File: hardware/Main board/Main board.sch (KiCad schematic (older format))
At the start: 104 parts, among them J1 Wind Direction, J10 Free Pins, J11 Nokia 5110 LCD, J12 3v3 in, J2 Wind Speed, J3 USB_B_Micro, J4 Micro_SD_Card, J5 Sensor board connector, J6 230V AC IN, J7 ISP programmer, J8 SPI1, J9 SPI2, Q1 IRLML2060, SW1 SW_Push, SW2 SW_SPST, SW3 SW_Push, SW4 SW_Push, SW5 Page Switch btn, U1 FT232RL, U2 MCP6042, U4 ATmega1284P-AU, U5 DS3231MZ, U6 ENC28J60, U7 USB6B1, U8 DRV5053, Y1 16MHZ

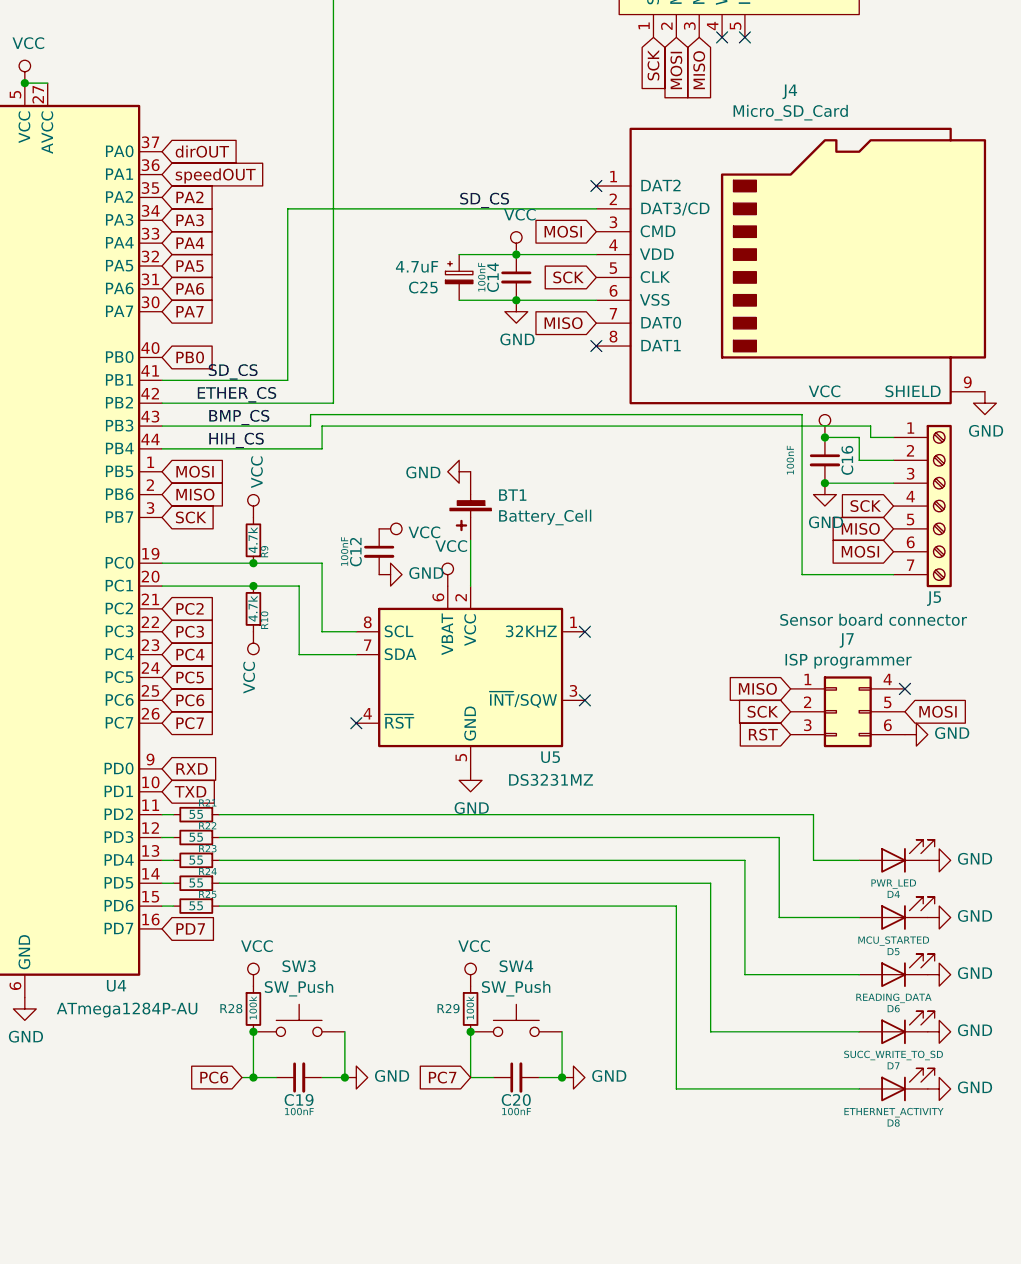
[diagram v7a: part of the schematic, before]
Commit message: Changed a few pins
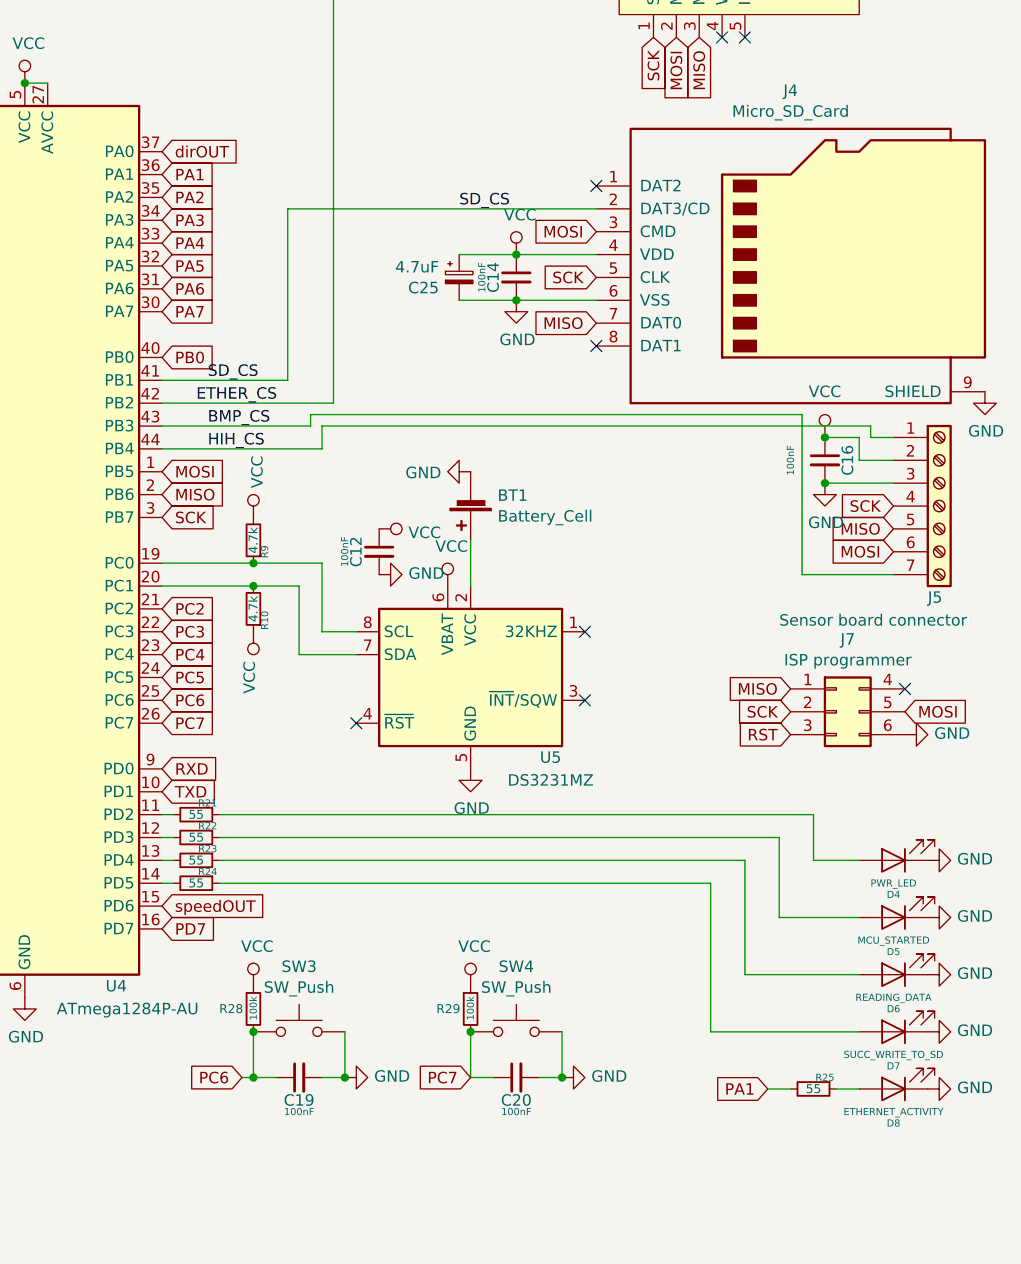
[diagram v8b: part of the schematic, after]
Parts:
- RV3: footprint Capacitor_SMD:C_0603_1608Metric_Pad1.05x0.95mm_HandSolder -> Meteo_Footprints:Varistor_SMD
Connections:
- net speedOUT: now also U4.15 (PD6); no longer U4.36 (PA1)
- net PA1: now reaches R25.2
- net PA1: now also U4.36 (PA1); no longer U4.15 (PD6)
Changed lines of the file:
@@
 Text GLabel 5150 1950 2    50   Input ~ 0
 speedOUT
-Text GLabel 7550 2350 2    50   Input ~ 0
+Text GLabel 7550 5550 2    50   Input ~ 0
 speedOUT
 $Comp
@@
 	0    1    1    0
 $EndComp
-$Comp
-L Device:R_Small R25
-U 1 1 5D4A70F7
-P 7700 5550
-F 0 "R25" V 7650 5600 31  0000 C CNN
-F 1 "55" V 7700 5550 39  0000 C CNN
-F 2 "Resistor_SMD:R_0805_2012Metric" H 7700 5550 50  0001 C CNN
-F 3 "~" H 7700 5550 50  0001 C CNN
-	1    7700 5550
-	0    1    1    0
-$EndComp
 Wire Wire Line
 	7550 5250 7600 5250
@@
 	7550 5450 7600 5450
 Wire Wire Line
-	7550 5550 7600 5550
-Wire Wire Line
 	7800 5150 10400 5150
 Wire Wire Line
@@
 Wire Wire Line
 	7800 5450 9950 5450
-Wire Wire Line
-	7800 5550 9800 5550
 $Comp
 L Device:D_Zener D1
@@
 Wire Wire Line
 	9950 6100 10600 6100
-Wire Wire Line
-	9800 6350 10600 6350
 $Comp
 L power:GND #PWR043
@@
 	7550 5150 7600 5150
 Wire Wire Line
-	9800 5550 9800 6350
-Wire Wire Line
 	9950 5450 9950 6100
 Wire Wire Line
@@
 F 0 "RV3" H 4703 1046 50  0000 L CNN
 F 1 "Varistor" H 4703 955 50  0000 L CNN
-F 2 "Capacitor_SMD:C_0603_1608Metric_Pad1.05x0.95mm_HandSolder" V 4530 1000 50  0001 C CNN
+F 2 "Meteo_Footprints:Varistor_SMD" V 4530 1000 50  0001 C CNN
 F 3 "~" H 4600 1000 50  0001 C CNN
 	1    4600 1000
@@
 	1    0    0    -1
 $EndComp
+Text GLabel 7550 2350 2    50   Input ~ 0
+PA1
+Text GLabel 10200 6350 0    50   Input ~ 0
+PA1
+$Comp
+L Device:R_Small R25
+U 1 1 5D423F75
+P 10400 6350
+F 0 "R25" V 10350 6400 31  0000 C CNN
+F 1 "55" V 10400 6350 39  0000 C CNN
+F 2 "Resistor_SMD:R_0805_2012Metric" H 10400 6350 50  0001 C CNN
+F 3 "~" H 10400 6350 50  0001 C CNN
+	1    10400 6350
+	0    1    1    0
+$EndComp
+Wire Wire Line
+	10600 6350 10500 6350
+Wire Wire Line
+	10300 6350 10200 6350
 $EndSCHEMATC
